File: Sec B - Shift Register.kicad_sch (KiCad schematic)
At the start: 6 parts, among them U2 STP16CP05M

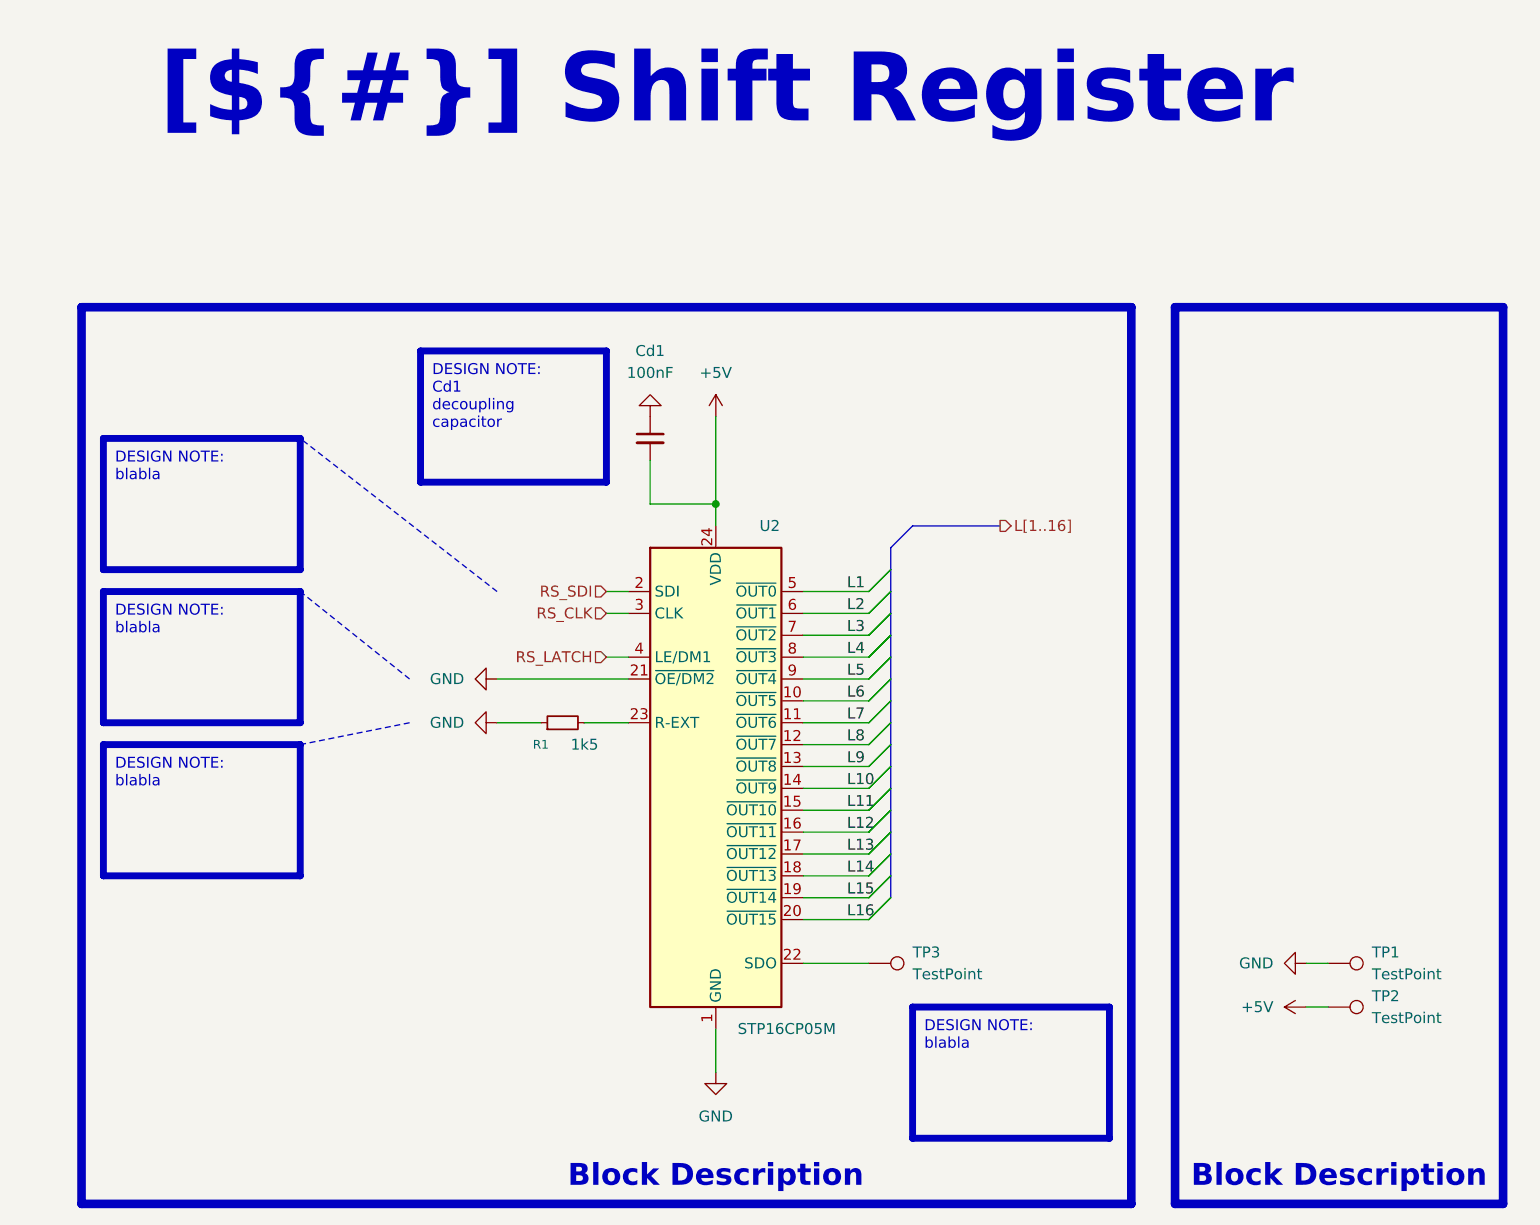
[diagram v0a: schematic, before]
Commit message: documentation update / release 2.1.1 prep
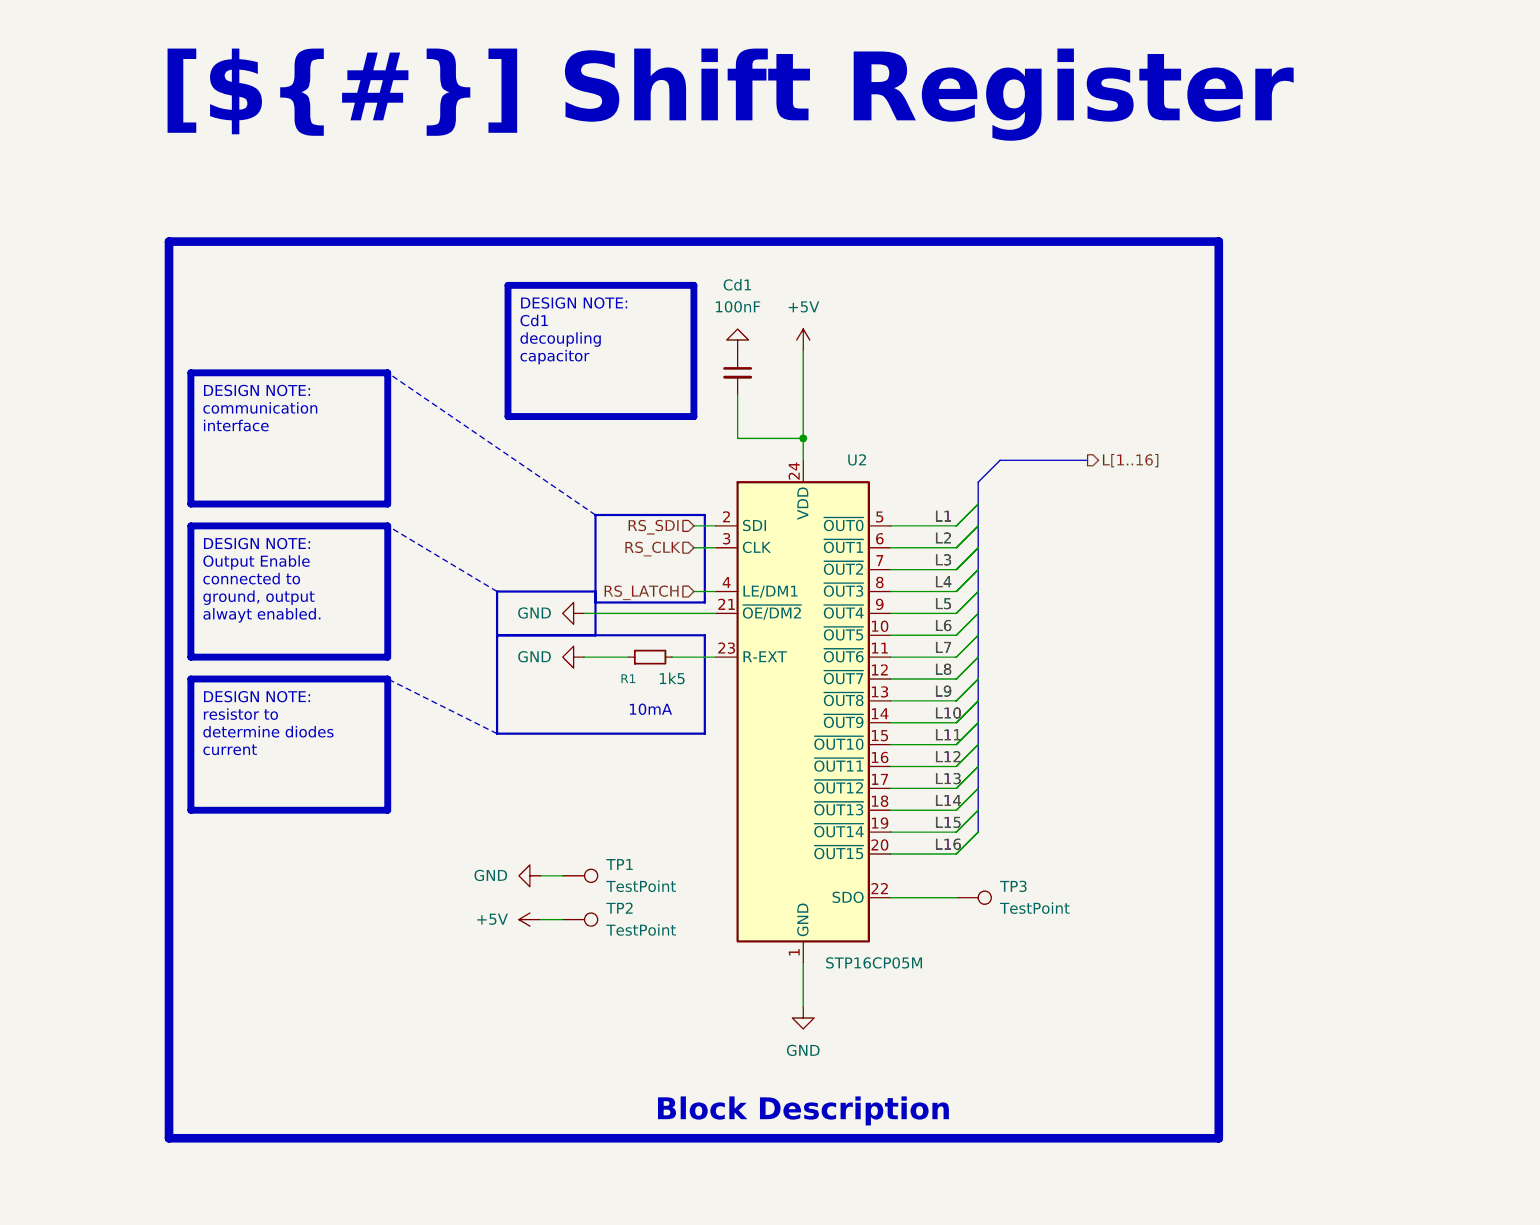
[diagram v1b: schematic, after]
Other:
- note added: "10mA"
- moved on the sheet: Cd1, R1, TP1, TP2, TP3, U2
